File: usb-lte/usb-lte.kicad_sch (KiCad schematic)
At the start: 40 parts, among them J1 Sim slot, P1 USB_C_Plug_USB2.0, Q1 BC847W, Q2 BC847W, U1 TPS62A02APDDC

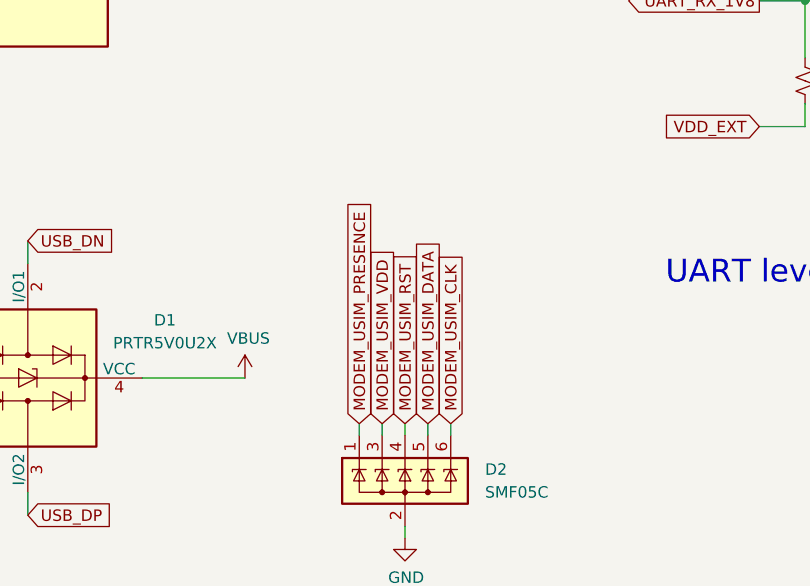
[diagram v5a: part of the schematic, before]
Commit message: Moved TVS diode closer to sim slot
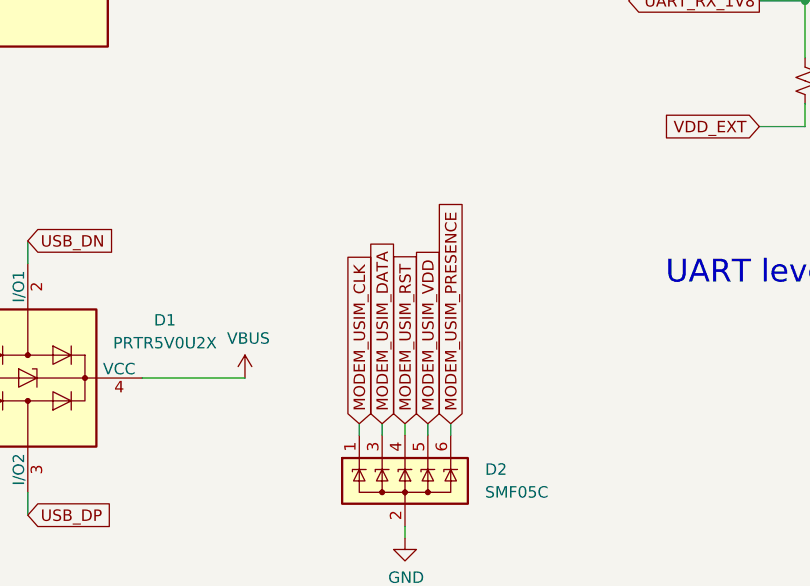
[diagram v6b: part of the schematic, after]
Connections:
- net MODEM_USIM_CLK: now also D2.1 (K); no longer D2.6 (K)
- net MODEM_USIM_DATA: now also D2.3 (K); no longer D2.5 (K)
- net MODEM_USIM_PRESENCE: now also D2.6 (K); no longer D2.1 (K)
- net MODEM_USIM_VDD: now also D2.5 (K); no longer D2.3 (K)
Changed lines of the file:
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@@
+		)
+	)
+	(global_label "MODEM_USIM_DATA"
+		(shape input)
+		(at 186.69 129.54 90)
+		(fields_autoplaced yes)
+		(effects
+			(font
+				(size 1.27 1.27)
+			)
+			(justify left)
+		)
+		(property "Intersheetrefs" "${INTERSHEET_REFS}"
+			(at 186.69 108.9563 90)
+			(effects
+				(font
+					(size 1.27 1.27)
+				)
+				(justify left)
+				(hide yes)
+			)
 		)
 	)
@@
 		)
 	)
+	(global_label "MODEM_USIM_VDD"
+		(shape input)
+		(at 191.77 129.54 90)
+		(fields_autoplaced yes)
+		(effects
+			(font
+				(size 1.27 1.27)
+			)
+			(justify left)
+		)
+		(property "Intersheetrefs" "${INTERSHEET_REFS}"
+			(at 191.77 109.7425 90)
+			(effects
+				(font
+					(size 1.27 1.27)
+				)
+				(justify left)
+				(hide yes)
+			)
+		)
+	)
 	(global_label "MODEM_USIM_RST"
 		(shape input)
@@
 	(global_label "MODEM_USIM_PRESENCE"
 		(shape input)
+		(at 194.31 129.54 90)
+		(fields_autoplaced yes)
+		(effects
+			(font
+				(size 1.27 1.27)
+			)
+			(justify left)
+		)
+		(property "Intersheetrefs" "${INTERSHEET_REFS}"
+			(at 194.31 103.5741 90)
+			(effects
+				(font
+					(size 1.27 1.27)
+				)
+				(justify left)
+				(hide yes)
+			)
+		)
+	)
+	(global_label "MODEM_USIM_VDD"
+		(shape input)
+		(at 121.92 52.07 180)
+		(fields_autoplaced yes)
+		(effects
+			(font
+				(size 1.27 1.27)
+			)
+			(justify right)
+		)
+		(property "Intersheetrefs" "${INTERSHEET_REFS}"
+			(at 102.1225 52.07 0)
+			(effects
+				(font
+					(size 1.27 1.27)
+				)
+				(justify right)
+				(hide yes)
+			)
+		)
+	)
+	(global_label "MODEM_USIM_CLK"
+		(shape input)
 		(at 184.15 129.54 90)
 		(fields_autoplaced yes)
@@
 		)
 		(property "Intersheetrefs" "${INTERSHEET_REFS}"
-			(at 184.15 103.5741 90)
-			(effects
-				(font
-					(size 1.27 1.27)
-				)
-				(justify left)
-				(hide yes)
-			)
-		)
-	)
-	(global_label "MODEM_USIM_VDD"
-		(shape input)
-		(at 121.92 52.07 180)
-		(fields_autoplaced yes)
-		(effects
-			(font
-				(size 1.27 1.27)
-			)
-			(justify right)
-		)
-		(property "Intersheetrefs" "${INTERSHEET_REFS}"
-			(at 102.1225 52.07 0)
-			(effects
-				(font
-					(size 1.27 1.27)
-				)
-				(justify right)
-				(hide yes)
-			)
-		)
-	)
-	(global_label "MODEM_USIM_CLK"
-		(shape input)
-		(at 194.31 129.54 90)
-		(fields_autoplaced yes)
-		(effects
-			(font
-				(size 1.27 1.27)
-			)
-			(justify left)
-		)
-		(property "Intersheetrefs" "${INTERSHEET_REFS}"
-			(at 194.31 109.803 90)
-			(effects
-				(font
-					(size 1.27 1.27)
-				)
-				(justify left)
-				(hide yes)
-			)
-		)
-	)
-	(global_label "MODEM_USIM_DATA"
-		(shape input)
-		(at 191.77 129.54 90)
-		(fields_autoplaced yes)
-		(effects
-			(font
-				(size 1.27 1.27)
-			)
-			(justify left)
-		)
-		(property "Intersheetrefs" "${INTERSHEET_REFS}"
-			(at 191.77 108.9563 90)
+			(at 184.15 109.803 90)
 			(effects
 				(font
@@
 				(hide yes)
 			)
-		)
-	)
-	(global_label "MODEM_USIM_VDD"
-		(shape input)
-		(at 186.69 129.54 90)
-		(fields_autoplaced yes)
-		(effects
-			(font
-				(size 1.27 1.27)
-			)
-			(justify left)
-		)
-		(property "Intersheetrefs" "${INTERSHEET_REFS}"
-			(at 186.69 109.7425 90)
-			(effects
-				(font
-					(size 1.27 1.27)
-				)
-				(justify left)
-				(hide yes)
-			)

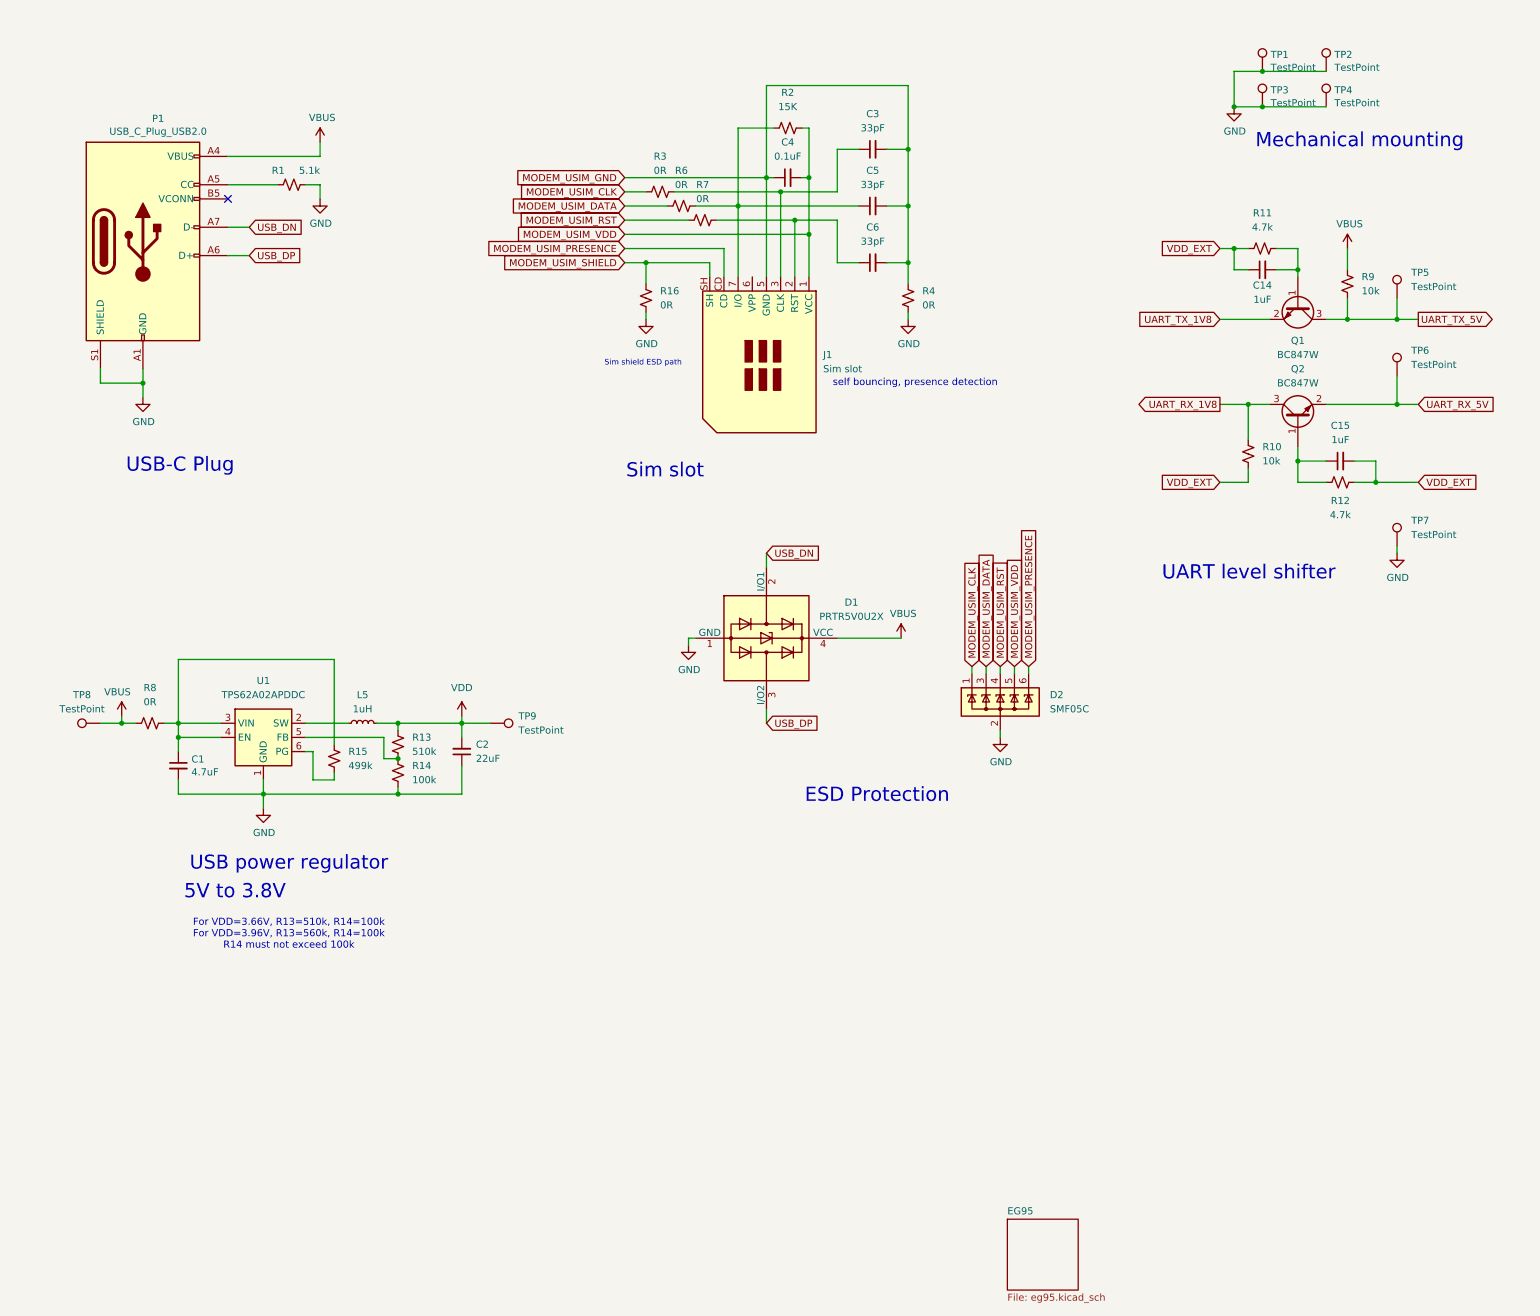
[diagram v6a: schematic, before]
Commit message: Add debug uart breakout
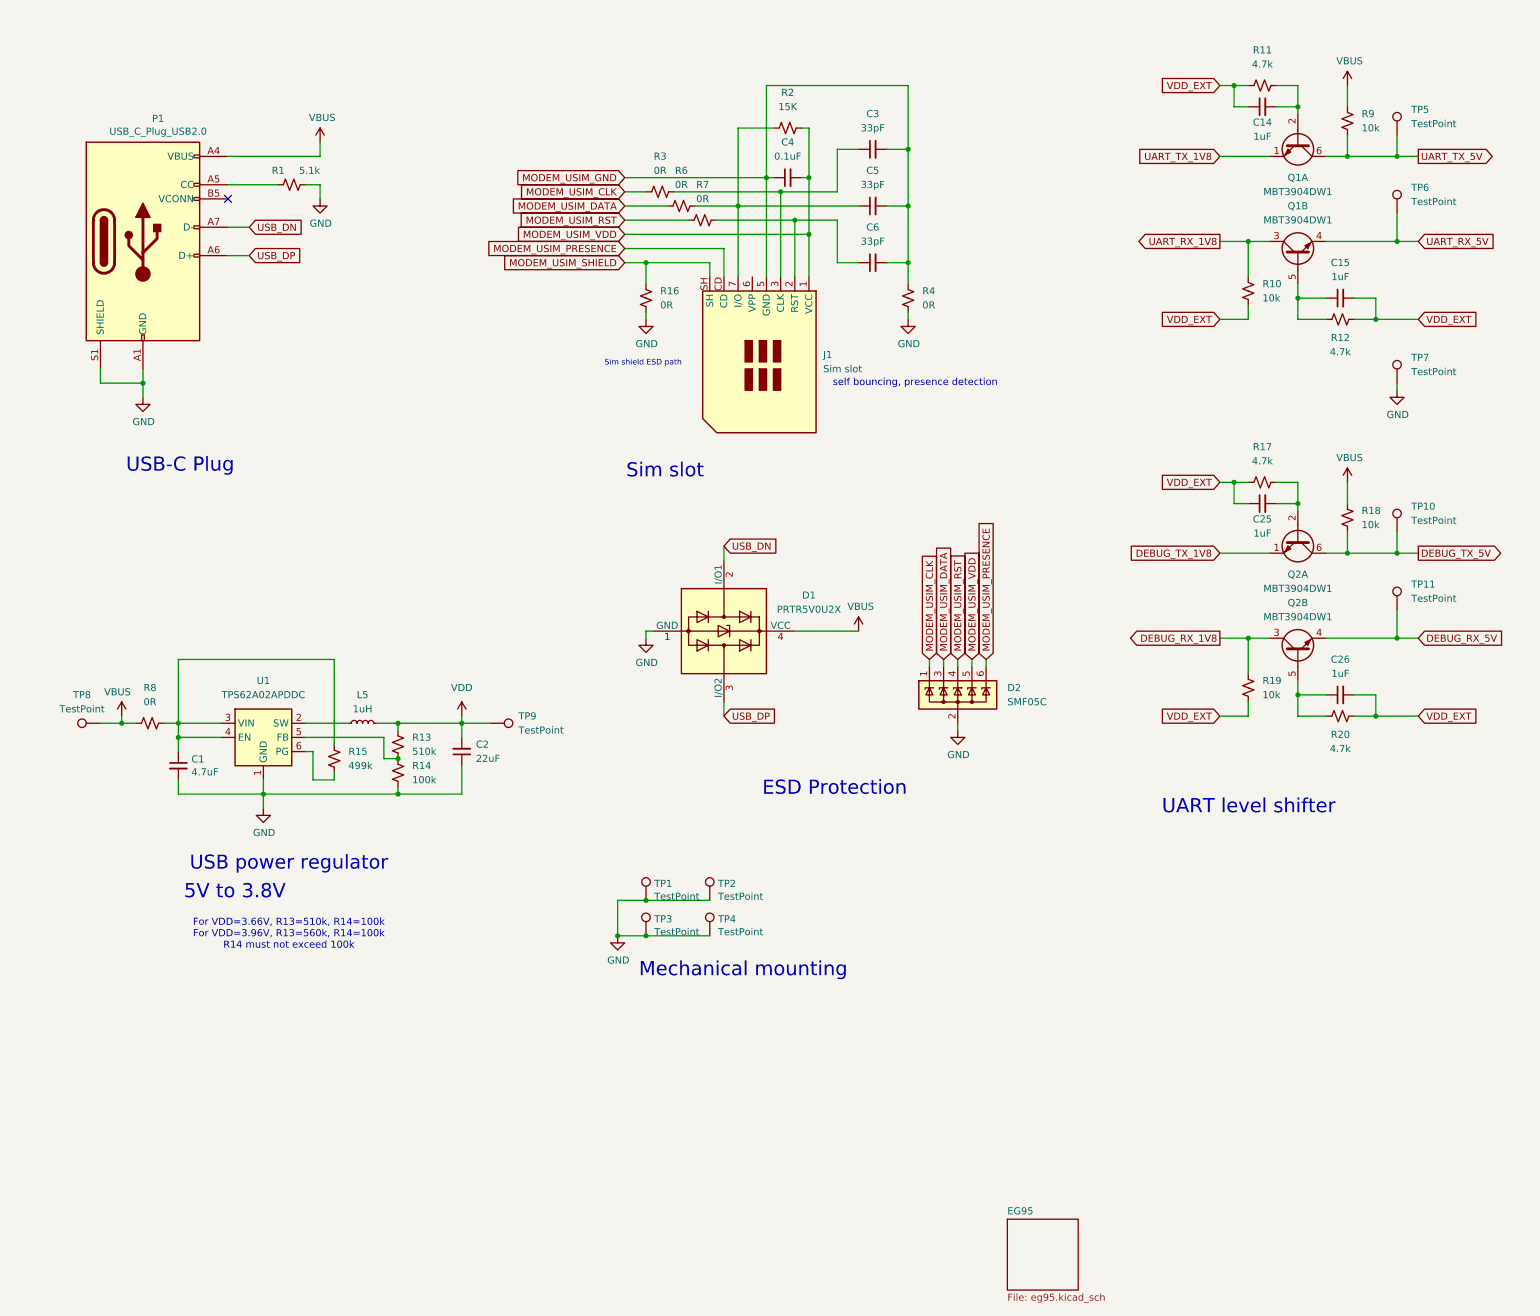
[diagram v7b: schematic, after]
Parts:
- removed Q1, Q2: BC847W, Package_TO_SOT_SMD:SOT-323_SC-70, symbol Transistor_BJT:BC847W
- added C25, C26: 1uF, Capacitor_SMD:C_0402_1005Metric, symbol Device:C_Small
- added Q1, Q2: MBT3904DW1, Package_TO_SOT_SMD:SOT-363_SC-70-6, symbol Transistor_BJT:MBT3904DW1
- added R17, R20: 4.7k, Resistor_SMD:R_0402_1005Metric, symbol Device:R_Small_US
- added R18, R19: 10k, Resistor_SMD:R_0402_1005Metric, symbol Device:R_Small_US
- added TP10, TP11: TestPoint, footprints:TestPoint_Pad_1mm, symbol Connector:TestPoint
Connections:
- net UART_RX_1V8: now also Q1.3 (C2)
- net UART_RX_5V: now also Q1.4 (E2)
- net UART_TX_1V8: now also Q1.1 (E1)
- net UART_TX_5V: now also Q1.6 (C1)
- net VBUS: now also R18.1
- net VDD_EXT: now also C25.1, C26.2, R17.1, R19.2, R20.2
- net at C15.1, R12.1: now also Q1.5 (B2)
- net at C14.2, R11.2: now also Q1.2 (B1)
- new net: C25.2, Q2.2 (B1), R17.2
- new net: C26.1, Q2.5 (B2), R20.1
- new net DEBUG_RX_1V8: Q2.3 (C2), R19.1
- new net DEBUG_RX_5V: Q2.4 (E2), TP11.1
- new net DEBUG_TX_1V8: Q2.1 (E1)
- new net DEBUG_TX_5V: Q2.6 (C1), R18.2, TP10.1
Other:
- moved on the sheet: C14, C15, D1, D2, R10, R11, R12, R9, TP1, TP2, TP3, TP4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

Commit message: Add status lights and usb boot key
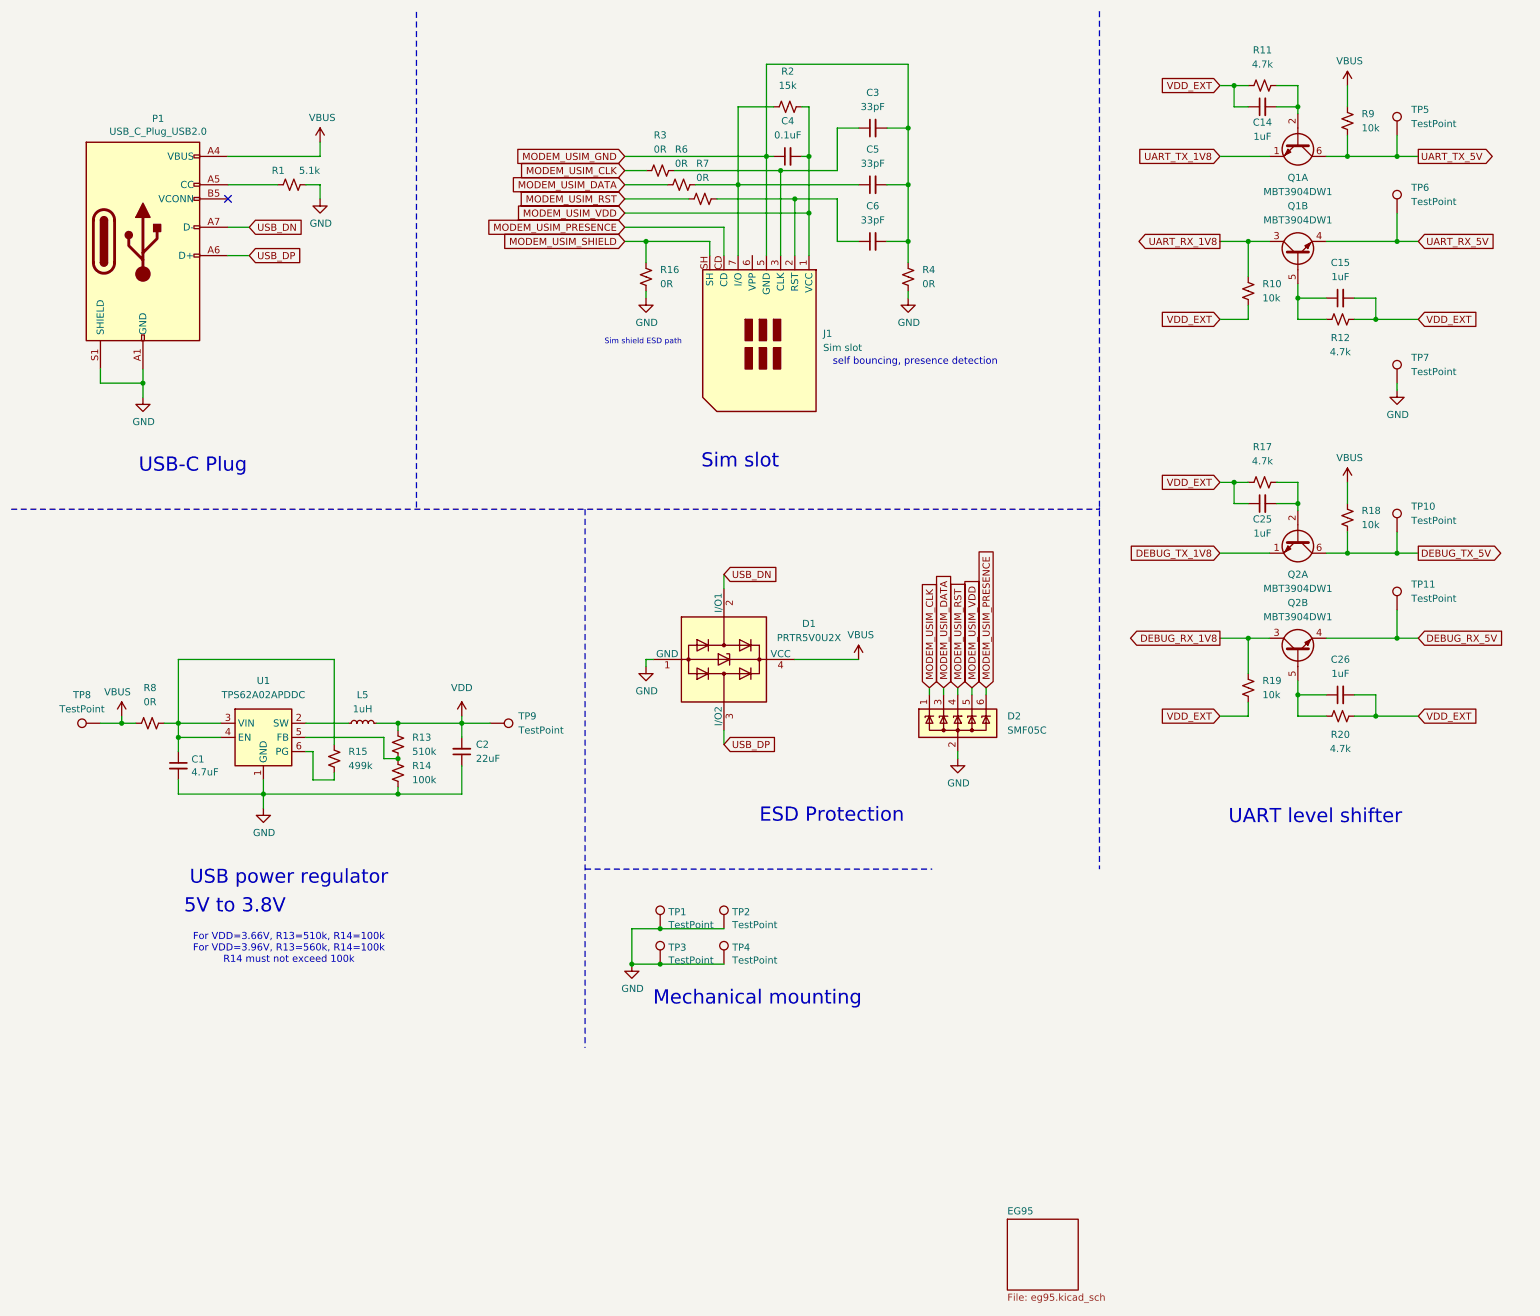
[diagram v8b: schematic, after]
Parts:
- R2: value 15K -> 15k
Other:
- title: Framework LTE Expansion Card -> Framework Cellular Expansion Card
- moved on the sheet: C3, C4, C5, C6, D1, D2, J1, R16, R2, R3, R4, R6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
